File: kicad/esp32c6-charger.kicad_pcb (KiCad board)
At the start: 2 copper layers, 160 x 50 mm, 22 parts, among them J1 Conn_01x02_Socket, J2 Power/Lock/Detect, J3 Relay, K1 G2RL-1, Q1 BC337, Q2 BC337, U1 AMS1117-5.0, U2 XIAO-ESP32-C6

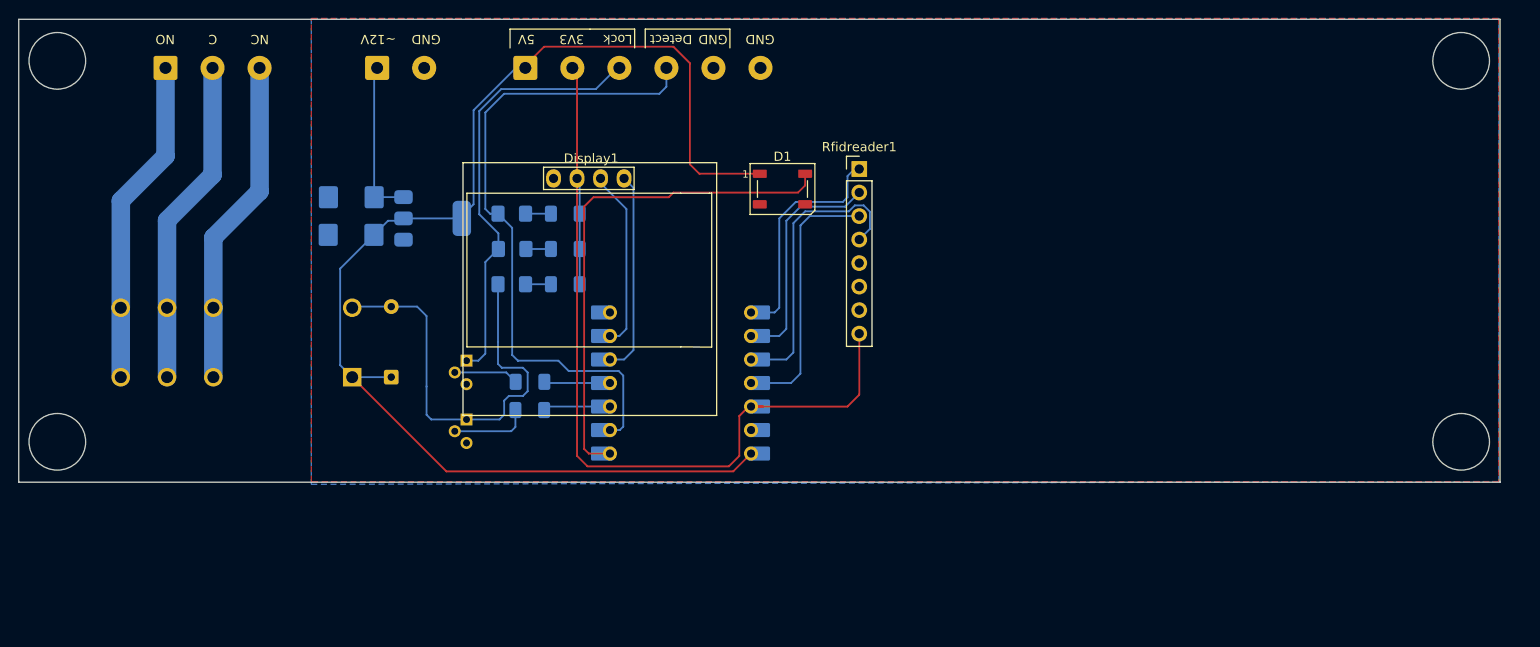
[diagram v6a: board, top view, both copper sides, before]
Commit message: THT Transistors instead of SMT, export jobs now include solder masks and automatically zips them up
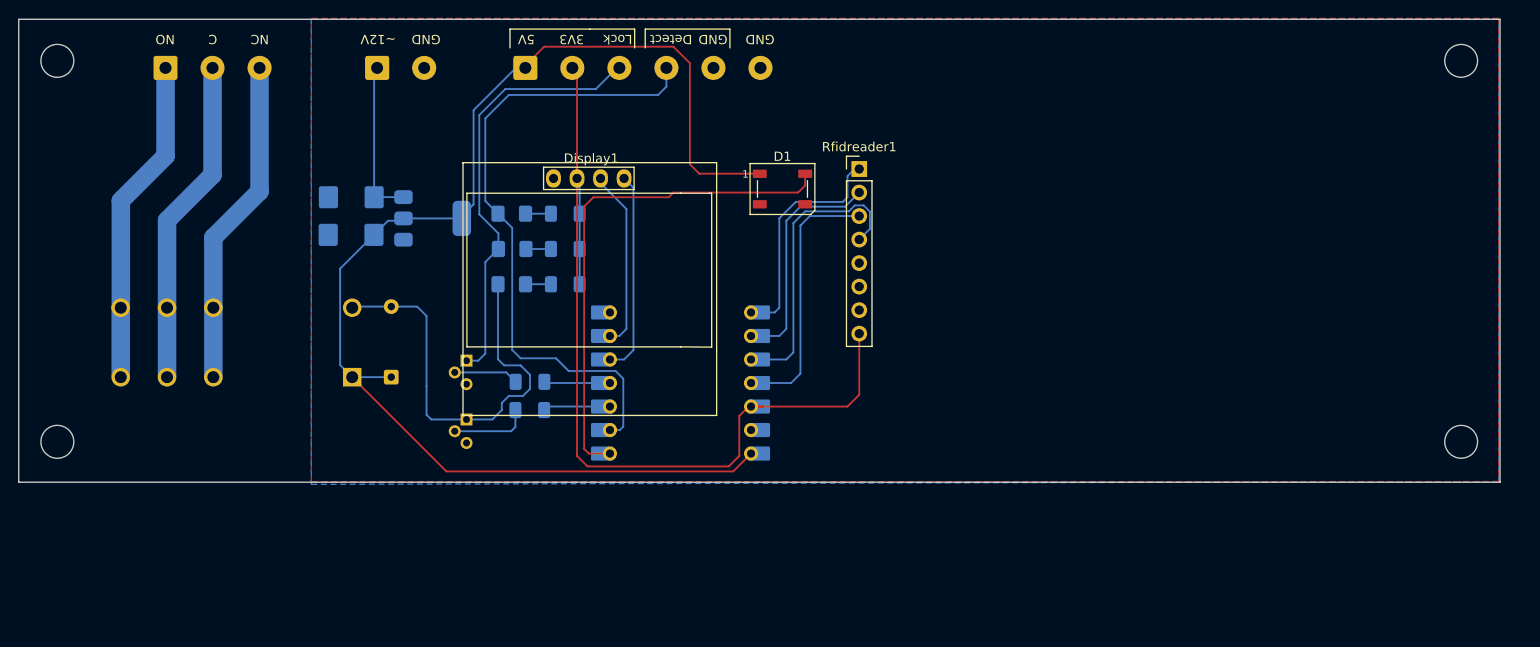
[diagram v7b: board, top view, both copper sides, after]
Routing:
- net /Detect: track 72.6 -> 71.2 mm
- net /Relay: track 46.7 -> 46.1 mm
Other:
- outline, holes or cut-outs redrawn
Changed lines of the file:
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@@
 	)
 	(gr_circle
-		(center 223.509435 120.015)
-		(end 226.557435 120.269)
+		(center 223.509435 78.867)
+		(end 221.742 78.74)
 		(stroke
 			(width 0.05)
@@
 		(layer "Edge.Cuts")
 	)
-	(gr_circle
-		(center 223.509435 78.867)
-		(end 226.557435 79.121)
-		(stroke
-			(width 0.05)
-			(type default)
-		)
-		(fill no)
-		(layer "Edge.Cuts")
-	)
-	(gr_circle
-		(center 71.882 78.867)
-		(end 74.93 79.121)
-		(stroke
-			(width 0.05)
-			(type default)
-		)
-		(fill no)
-		(layer "Edge.Cuts")
-	)
 	(gr_line
 		(start 227.714 74.379)
@@
 		(layer "Edge.Cuts")
 	)
+	(gr_circle
+		(center 223.509435 120.015)
+		(end 221.742 119.888)
+		(stroke
+			(width 0.05)
+			(type default)
+		)
+		(fill no)
+		(layer "Edge.Cuts")
+	)
 	(gr_line
 		(start 67.714 74.379)
@@
 		(layer "Edge.Cuts")
 	)
+	(gr_circle
+		(center 71.882 120.015)
+		(end 70.104 120.015)
+		(stroke
+			(width 0.05)
+			(type default)
+		)
+		(fill no)
+		(layer "Edge.Cuts")
+	)
 	(gr_line
 		(start 227.714 74.379)
@@
 	)
 	(gr_circle
-		(center 71.882 120.015)
-		(end 74.93 120.269)
+		(center 71.882 78.867)
+		(end 70.104 78.867)
 		(stroke
 			(width 0.05)
@@
 	)
 	(segment
-		(start 117.455 84.2889)
-		(end 117.455 95.441894)
-		(width 0.2)
-		(layer "B.Cu")
-		(net 5)
-	)
-	(segment
-		(start 130.048 81.915)
-		(end 119.8289 81.915)
+		(start 117.455 95.441894)
+		(end 119.521935 97.508829)
 		(width 0.2)
 		(layer "B.Cu")
@@
 	)
 	(segment
+		(start 117.455 84.729)
+		(end 117.455 95.441894)
+		(width 0.2)
+		(layer "B.Cu")
+		(net 5)
+	)
+	(segment
 		(start 118.11 110.49)
 		(end 117.348 111.252)
@@
 	)
 	(segment
+		(start 119.521935 97.508829)
+		(end 119.521935 99.187)
+		(width 0.2)
+		(layer "B.Cu")
+		(net 5)
+	)
+	(segment
+		(start 120.269 81.915)
+		(end 117.455 84.729)
+		(width 0.2)
+		(layer "B.Cu")
+		(net 5)
+	)
+	(segment
 		(start 119.521935 99.187)
 		(end 118.11 100.598935)
@@
 	)
 	(segment
-		(start 117.455 95.441894)
-		(end 119.521935 97.508829)
-		(width 0.2)
-		(layer "B.Cu")
-		(net 5)
-	)
-	(segment
-		(start 119.8289 81.915)
-		(end 117.455 84.2889)
+		(start 130.048 81.915)
+		(end 120.269 81.915)
 		(width 0.2)
 		(layer "B.Cu")
@@
 	)
 	(segment
-		(start 119.521935 97.508829)
-		(end 119.521935 99.187)
-		(width 0.2)
-		(layer "B.Cu")
-		(net 5)
-	)
-	(segment
 		(start 120.904 118.872)
 		(end 114.808 118.872)
@@
 	)
 	(segment
+		(start 120.142 111.76)
+		(end 121.92 111.76)
+		(width 0.2)
+		(layer "B.Cu")
+		(net 8)
+	)
+	(segment
+		(start 122.936 112.776)
+		(end 122.936 114.3)
+		(width 0.2)
+		(layer "B.Cu")
+		(net 8)
+	)
+	(segment
+		(start 119.888 116.586)
+		(end 118.872 117.602)
+		(width 0.2)
+		(layer "B.Cu")
+		(net 8)
+	)
+	(segment
+		(start 118.872 117.602)
+		(end 116.078 117.602)
+		(width 0.2)
+		(layer "B.Cu")
+		(net 8)
+	)
+	(segment
 		(start 112.268 117.602)
 		(end 111.76 117.094)
@@
 	)
 	(segment
-		(start 119.479 109.22)
-		(end 119.479 111.605)
-		(width 0.2)
-		(layer "B.Cu")
-		(net 8)
-	)
-	(segment
-		(start 120.142 117.094)
-		(end 119.634 117.602)
-		(width 0.2)
-		(layer "B.Cu")
-		(net 8)
-	)
-	(segment
-		(start 122.682 112.522)
-		(end 122.682 114.554)
-		(width 0.2)
-		(layer "B.Cu")
-		(net 8)
-	)
-	(segment
-		(start 122.174 112.014)
-		(end 122.682 112.522)
-		(width 0.2)
-		(layer "B.Cu")
-		(net 8)
-	)
-	(segment
-		(start 122.682 114.554)
-		(end 122.174 115.062)
-		(width 0.2)
-		(layer "B.Cu")
-		(net 8)
-	)
-	(segment
 		(start 111.76 114.046)
 		(end 111.76 106.426)
@@
 	)
 	(segment
-		(start 119.479 111.605)
-		(end 119.888 112.014)
-		(width 0.2)
-		(layer "B.Cu")
-		(net 8)
-	)
-	(segment
-		(start 120.142 115.57)
-		(end 120.142 117.094)
+		(start 119.479 111.097)
+		(end 120.142 111.76)
 		(width 0.2)
 		(layer "B.Cu")
@@
 	(segment
 		(start 120.65 115.062)
-		(end 120.142 115.57)
+		(end 119.888 115.824)
 		(width 0.2)
 		(layer "B.Cu")
@@
 	(segment
 		(start 119.479 102.997)
-		(end 119.479 109.22)
+		(end 119.479 111.097)
 		(width 0.2)
 		(layer "B.Cu")
@@
 	)
 	(segment
-		(start 119.888 112.014)
-		(end 122.174 112.014)
-		(width 0.2)
-		(layer "B.Cu")
-		(net 8)
-	)
-	(segment
-		(start 119.634 117.602)
-		(end 116.078 117.602)
+		(start 119.888 115.824)
+		(end 119.888 116.586)
+		(width 0.2)
+		(layer "B.Cu")
+		(net 8)
+	)
+	(segment
+		(start 122.936 114.3)
+		(end 122.174 115.062)
+		(width 0.2)
+		(layer "B.Cu")
+		(net 8)
+	)
+	(segment
+		(start 121.92 111.76)
+		(end 122.936 112.776)
 		(width 0.2)
 		(layer "B.Cu")
@@
 	)
 	(segment
-		(start 121.009435 110.638565)
-		(end 121.62287 111.252)
-		(width 0.2)
-		(layer "B.Cu")
-		(net 27)
-	)
-	(segment
 		(start 127.11379 112.367)
-		(end 125.99879 111.252)
+		(end 125.74479 110.998)
+		(width 0.2)
+		(layer "B.Cu")
+		(net 27)
+	)
+	(segment
+		(start 121.009435 110.087435)
+		(end 121.009435 96.907435)
+		(width 0.2)
+		(layer "B.Cu")
+		(net 27)
+	)
+	(segment
+		(start 130.737 118.745)
+		(end 132.631435 118.745)
+		(width 0.2)
+		(layer "B.Cu")
+		(net 27)
+	)
+	(segment
+		(start 121.009435 96.907435)
+		(end 119.479 95.377)
+		(width 0.2)
+		(layer "B.Cu")
+		(net 27)
+	)
+	(segment
+		(start 133.009435 113.197435)
+		(end 132.179 112.367)
+		(width 0.2)
+		(layer "B.Cu")
+		(net 27)
+	)
+	(segment
+		(start 133.009435 118.367)
+		(end 133.009435 113.197435)
+		(width 0.2)
+		(layer "B.Cu")
+		(net 27)
+	)
+	(segment
+		(start 120.65 82.55)
+		(end 118.11 85.09)
+		(width 0.2)
+		(layer "B.Cu")
+		(net 27)
+	)
+	(segment
+		(start 137.668 81.661)
+		(end 136.779 82.55)
+		(width 0.2)
+		(layer "B.Cu")
+		(net 27)
+	)
+	(segment
+		(start 118.11 85.09)
+		(end 118.11 94.008)
+		(width 0.2)
+		(layer "B.Cu")
+		(net 27)
+	)
+	(segment
+		(start 118.11 94.008)
+		(end 119.479 95.377)
+		(width 0.2)
+		(layer "B.Cu")
+		(net 27)
+	)
+	(segment
+		(start 125.74479 110.998)
+		(end 121.92 110.998)
+		(width 0.2)
+		(layer "B.Cu")
+		(net 27)
+	)
+	(segment
+		(start 121.92 110.998)
+		(end 121.009435 110.087435)
 		(width 0.2)
 		(layer "B.Cu")
@@
 	)
 	(segment
-		(start 136.906 82.423)
-		(end 120.142 82.423)
-		(width 0.2)
-		(layer "B.Cu")
-		(net 27)
-	)
-	(segment
-		(start 121.62287 111.252)
-		(end 121.666 111.252)
-		(width 0.2)
-		(layer "B.Cu")
-		(net 27)
-	)
-	(segment
-		(start 125.99879 111.252)
-		(end 121.666 111.252)
-		(width 0.2)
-		(layer "B.Cu")
-		(net 27)
-	)
-	(segment
-		(start 130.737 118.745)
-		(end 132.631435 118.745)
-		(width 0.2)
-		(layer "B.Cu")
-		(net 27)
-	)
-	(segment
-		(start 118.618 95.377)
-		(end 119.479 95.377)
-		(width 0.2)
-		(layer "B.Cu")
-		(net 27)
-	)
-	(segment
-		(start 121.009435 110.638565)
-		(end 121.009435 96.907435)
-		(width 0.2)
-		(layer "B.Cu")
-		(net 27)
-	)
-	(segment
-		(start 118.11 94.869)
-		(end 118.618 95.377)
-		(width 0.2)
-		(layer "B.Cu")
-		(net 27)
-	)
-	(segment
-		(start 121.009435 96.907435)
-		(end 119.479 95.377)
-		(width 0.2)
-		(layer "B.Cu")
-		(net 27)
-	)
-	(segment
-		(start 133.009435 118.367)
-		(end 133.009435 112.867)
-		(width 0.2)
-		(layer "B.Cu")
-		(net 27)
-	)
-	(segment
-		(start 118.11 84.455)
-		(end 118.11 94.869)
-		(width 0.2)
-		(layer "B.Cu")
-		(net 27)
-	)
-	(segment
-		(start 133.009435 112.867)
-		(end 132.509435 112.367)
+		(start 132.179 112.367)
+		(end 127.11379 112.367)
 		(width 0.2)
 		(layer "B.Cu")
@@
 	)
 	(segment
-		(start 137.668 81.661)
-		(end 136.906 82.423)
-		(width 0.2)
-		(layer "B.Cu")
-		(net 27)
-	)
-	(segment
-		(start 120.142 82.423)
-		(end 118.11 84.455)
-		(width 0.2)
-		(layer "B.Cu")
-		(net 27)
-	)
-	(segment
-		(start 132.509435 112.367)
-		(end 127.11379 112.367)
-		(width 0.2)
-		(layer "B.Cu")
+		(start 136.779 82.55)
+		(end 120.65 82.55)
+		(width 0.2)
+		(layer "B.Cu")
